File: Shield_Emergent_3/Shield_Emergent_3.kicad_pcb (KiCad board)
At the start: 2 copper layers, 17 parts, among them J1 USB3_B_Micro, J2 Conn_02x08_Odd_Even, J3 USB3_B_Micro, U3 SP3012-06UTG, U4 SP3012-06UTG, X1 USB_C_24pins

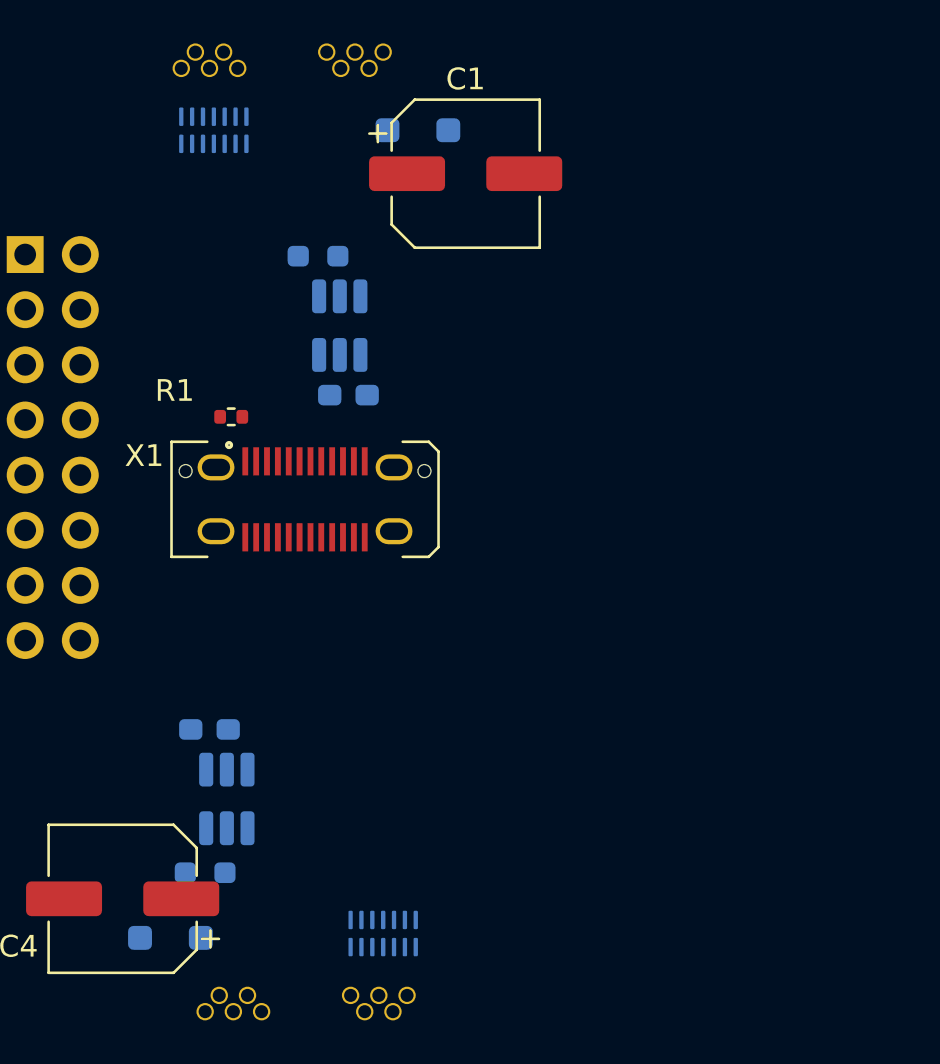
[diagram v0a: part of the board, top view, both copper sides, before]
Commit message: v0.7 nets were modified footprints were corrected Rdy 4 decomposition.
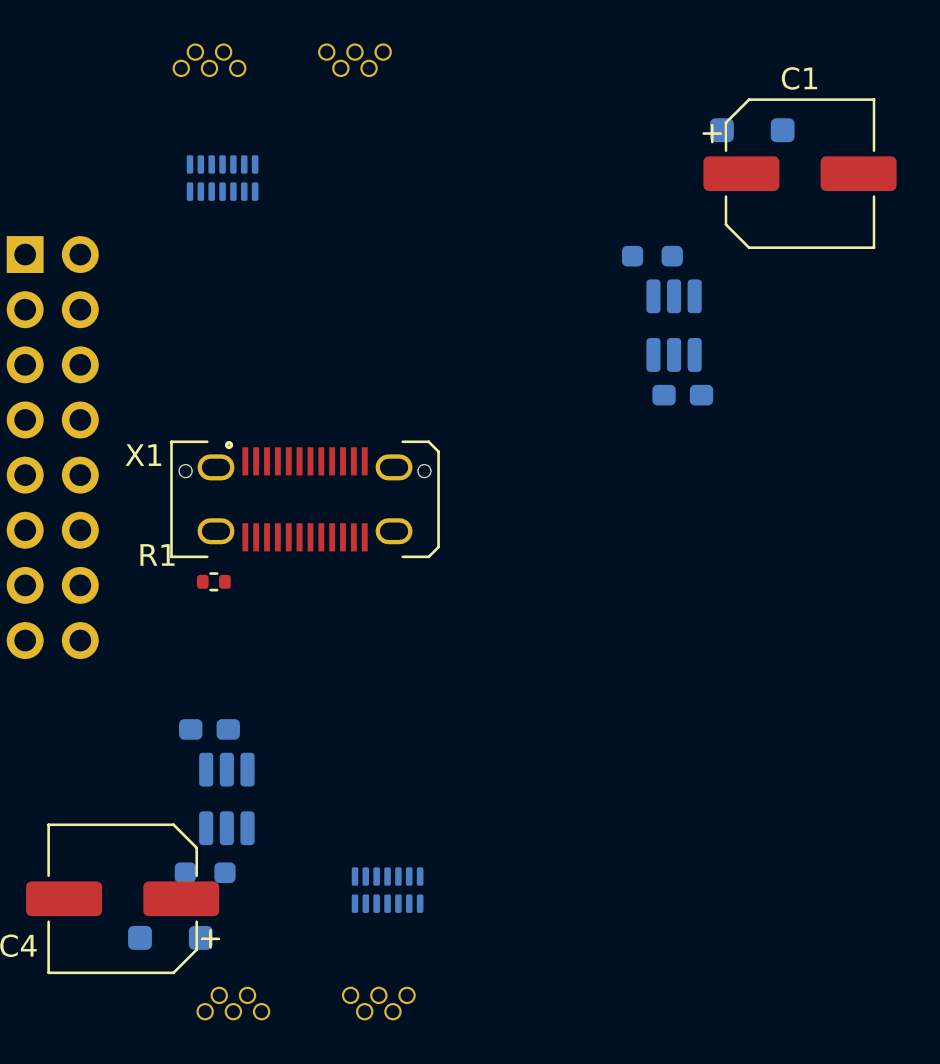
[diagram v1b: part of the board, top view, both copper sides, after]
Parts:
- U3, U4: footprint Package_DFN_QFN:DFN-14_1.35x3.5mm_P0.5mm -> myLib8:DFN-14_1.35x3.5mm_P0.5mm
- moved C1 15.4 mm to (110.4, 25.6)
- moved C2 15.4 mm to (105.0, 35.8)
- moved D1 15.4 mm to (108.2, 23.6)
- moved R4 15.4 mm to (103.6, 29.4)
- moved U1 15.4 mm to (104.6, 32.6)
- moved R1 7.64 mm to (83.4, 44.4)
- moved U3 2.24 mm to (83.8, 25.8)
- moved U4 2.01 mm to (91.4, 58.6)
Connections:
- U3 pad 1: TX1+ -> RX1+
- U3 pad 11: RX1- -> TX1-
- U3 pad 12: RX1+ -> TX1+
- U3 pad 13: TX1- -> RX1-
- U3 pad 14: TX1+ -> RX1+
- U3 pad 2: TX1- -> RX1-
- U3 pad 3: RX1+ -> TX1+
- U3 pad 4: RX1- -> TX1-
- U4 pad 1: TX2+ -> TX2-
- U4 pad 13: TX2- -> TX2+
- U4 pad 14: TX2+ -> TX2-
- U4 pad 2: TX2- -> TX2+

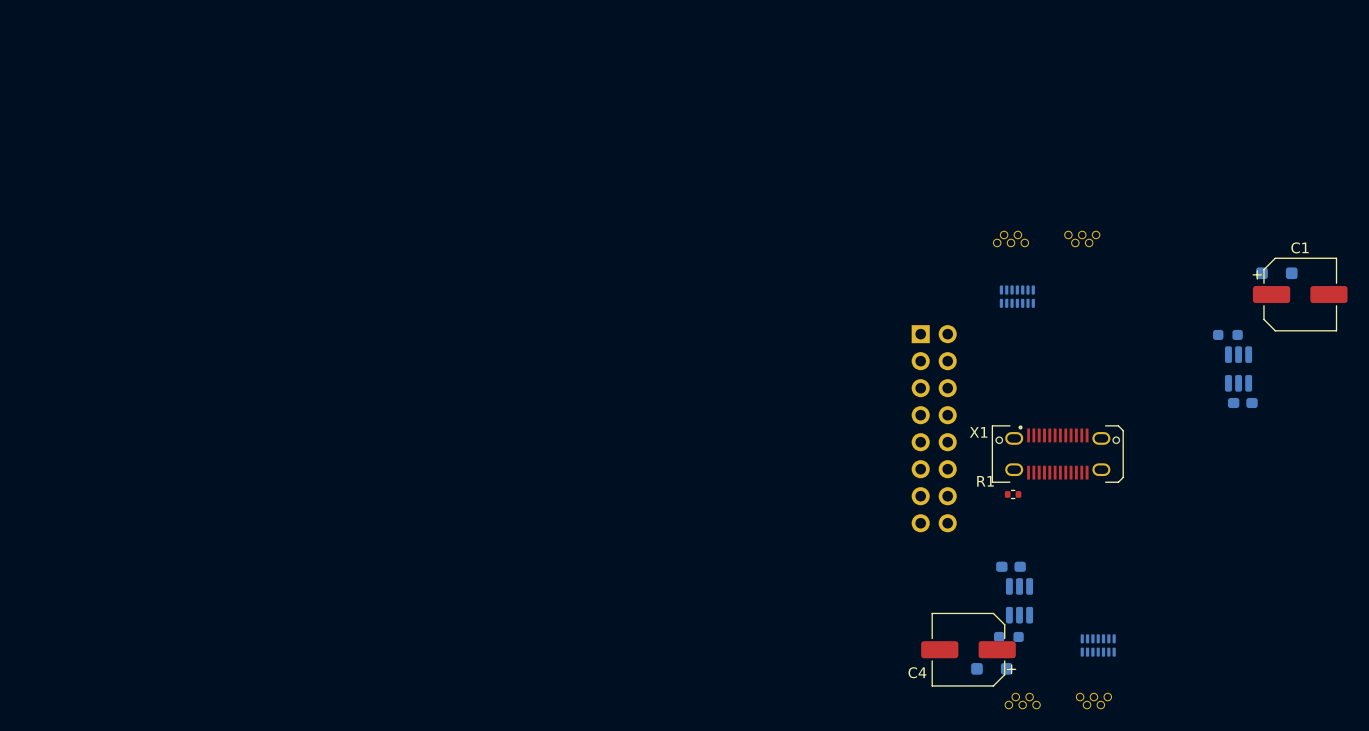
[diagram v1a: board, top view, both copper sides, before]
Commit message: v0.8 Partial decomposition was completed
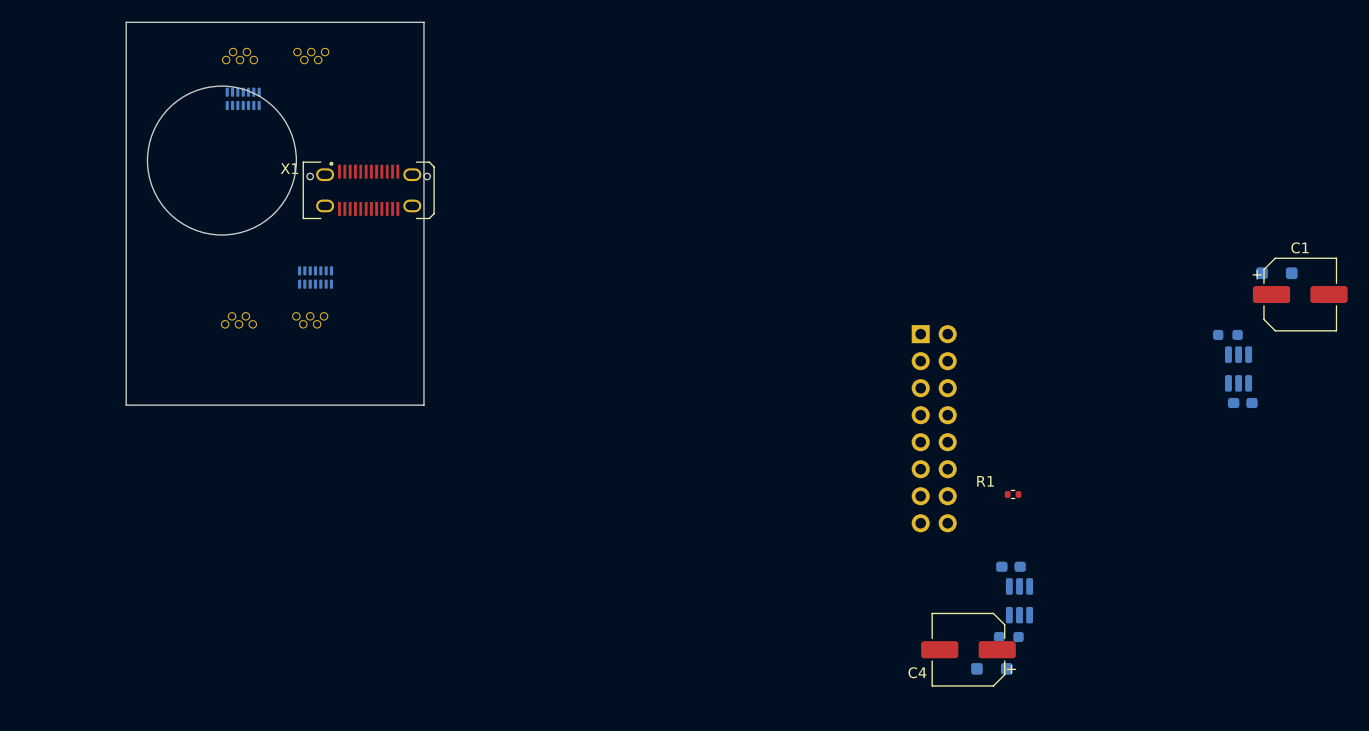
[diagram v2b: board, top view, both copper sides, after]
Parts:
- moved J3 81.9 mm to (9.30, 28.4)
- moved U4 81.3 mm to (17.8, 24.0), turned to 90 degrees
- moved U3 75.1 mm to (11.0, 7.20)
- moved J1 74.5 mm to (18.7, 2.80)
- moved X1 69.4 mm to (22.8, 15.8)
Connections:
- J3 pad 6: TX2- -> TX2+
- J3 pad 7: TX2+ -> TX2-
- U4 pad 1: TX2- -> RX2+
- U4 pad 11: RX2- -> TX2+
- U4 pad 12: RX2+ -> TX2-
- U4 pad 13: TX2+ -> RX2-
- U4 pad 14: TX2- -> RX2+
- U4 pad 2: TX2+ -> RX2-
- U4 pad 3: RX2+ -> TX2-
- U4 pad 4: RX2- -> TX2+
- X1 pad B2: TX2+ -> TX2-
- X1 pad B3: TX2- -> TX2+
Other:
- board outline added: 28 x 36 mm

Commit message: v0.9 Decomposition seems 2B completed
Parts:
- J2: value Conn_02x08_Odd_Even -> Conn_02x04_Odd_Even; footprint Connector_PinSocket_2.54mm:PinSocket_2x08_P2.54mm_Vertical -> Connector_PinHeader_2.54mm:PinHeader_2x04_P2.54mm_Vertical
- moved R4 90.0 mm to (16.2, 7.80), turned to -90 degrees
- moved D1 88.8 mm to (22.0, 2.40), turned to 90 degrees
- moved U1 88.7 mm to (19.4, 7.80), turned to 180 degrees
- moved C1 88.4 mm to (24.4, 5.20), turned to -90 degrees
- moved C2 87.0 mm to (22.6, 7.80), turned to -90 degrees
- moved U2 86.3 mm to (3.00, 24.6)
- moved C3 86.1 mm to (2.40, 21.4)
- moved R8 84.7 mm to (3.80, 27.8), turned to 0 degrees
- moved D2 83.6 mm to (6.00, 24.6), turned to 90 degrees
- moved C4 80.4 mm to (3.80, 31.0), turned to -90 degrees
- moved R1 62.1 mm to (26.6, 19.4), turned to 180 degrees
- moved J2 49.3 mm to (25.9, 22.8)
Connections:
- J2 pad 1: VBUS -> VOUT1
- J2 pad 2: VBUS -> VOUT2
- J2 pad 3: VBUS -> EN1
- J2 pad 4: VBUS -> EN2
- J2 pad 5: GND -> nFLT1
- J2 pad 6: GND -> nFLT2
- J2 pad 7: GND -> BTN1
- J2 pad 8: GND -> BTN2

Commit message: v1.0 Geometry was modified
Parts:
- C2, C3, D1, D2, R4, R8, U1, U2: moved to F.Cu
- moved C1 30.8 mm to (-6.40, 4.40)
- moved J2 16.1 mm to (19.4, 37.5), turned to -90 degrees
- moved C4 15.1 mm to (15.8, 21.8)
- moved C3 10.0 mm to (3.20, 31.4), turned to -90 degrees
- moved R1 8.40 mm to (18.4, 21.2), turned to -90 degrees
- moved U2 7.87 mm to (6.60, 31.6), turned to 0 degrees
- moved R8 7.62 mm to (10.4, 31.6), turned to -90 degrees
- moved C2 6.40 mm to (16.2, 7.80)
- moved R4 6.40 mm to (22.6, 7.80)
- moved J1 4.75 mm to (23.3, 1.60)
- moved U3 4.44 mm to (15.4, 7.80)
- moved D1 2.33 mm to (23.2, 4.40), turned to 0 degrees
- moved X1 2.24 mm to (22.4, 18.0), turned to -90 degrees
- moved D2 1.34 mm to (7.20, 24.0), turned to 180 degrees
- moved U4 0.82 mm to (17.0, 23.8)
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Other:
- board size 28 x 36 mm -> 23.6 x 33.6 mm

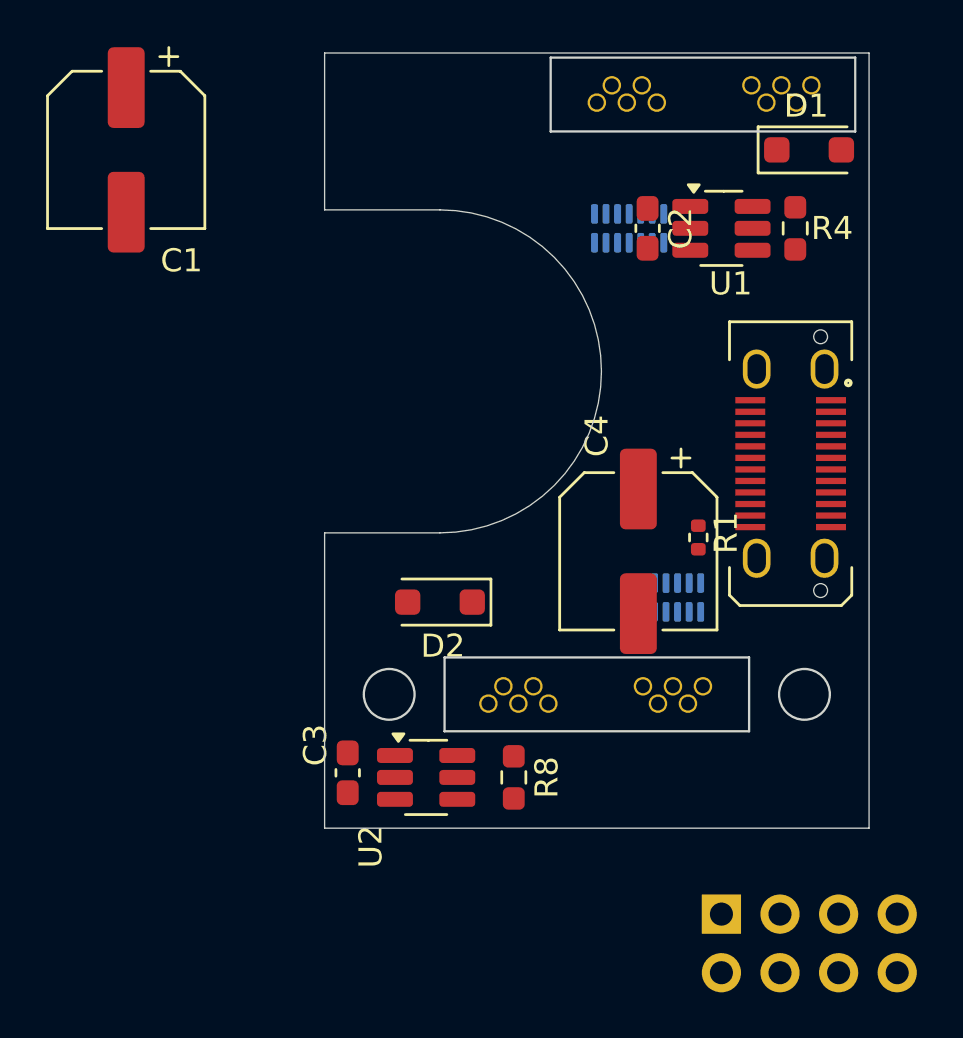
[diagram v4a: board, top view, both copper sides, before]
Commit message: v1.1 Geometry was established, LF routing was completed
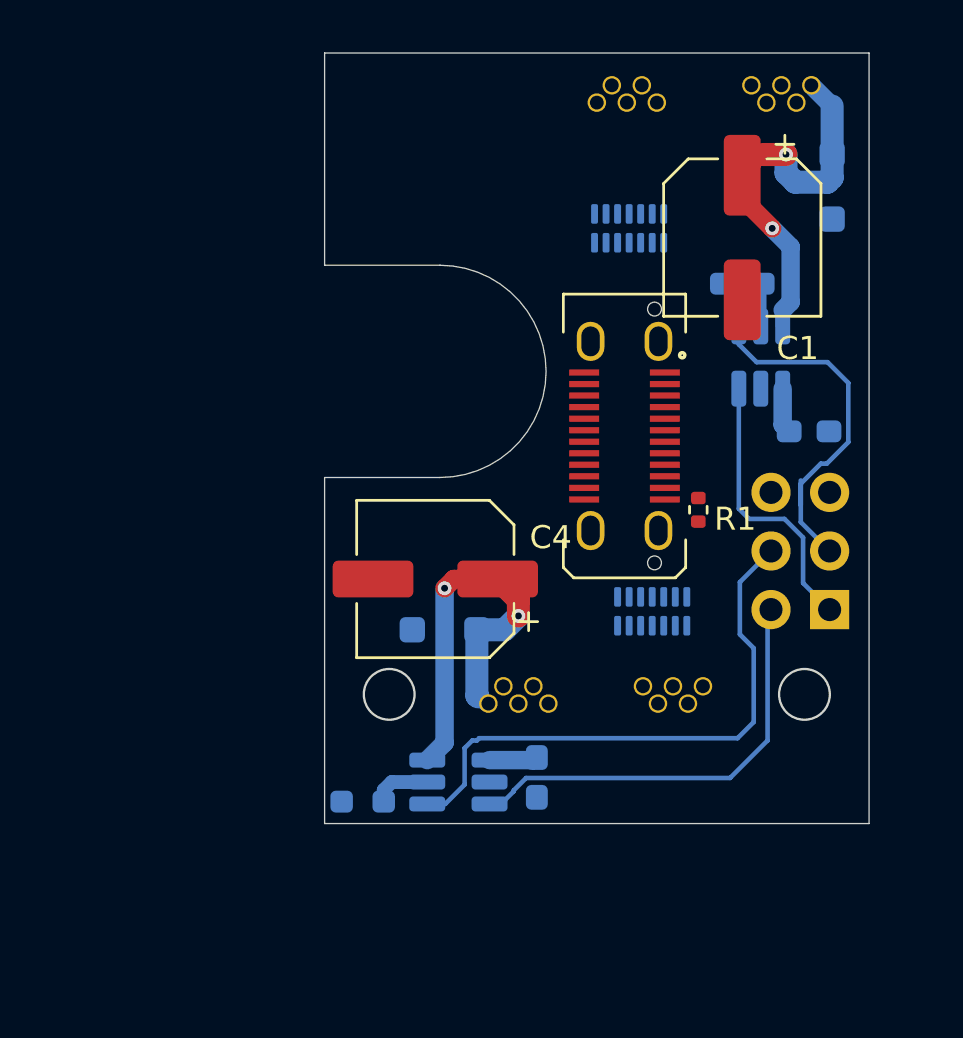
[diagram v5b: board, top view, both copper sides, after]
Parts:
- C2, C3, D1, D2, R4, R8, U1, U2: moved to B.Cu
- J2: value Conn_02x04_Odd_Even -> Conn_02x03_Odd_Even; footprint Connector_PinHeader_2.54mm:PinHeader_2x04_P2.54mm_Vertical -> Connector_PinSocket_2.54mm:PinSocket_2x03_P2.54mm_Vertical
- moved C1 27.0 mm to (20.3, 8.20)
- moved J2 14.0 mm to (24.1, 24.3), turned to 0 degrees
- moved C2 11.2 mm to (23.2, 16.6), turned to 0 degrees
- moved C4 8.88 mm to (7.00, 23.0), turned to 180 degrees
- moved C3 8.20 mm to (11.4, 31.6)
- moved X1 7.30 mm to (15.2, 16.8)
- moved R8 6.63 mm to (3.85, 32.6), turned to 180 degrees
- moved U1 5.85 mm to (21.1, 13.4), turned to 90 degrees
- moved R4 3.32 mm to (20.3, 10.2), turned to 180 degrees
- moved D1 1.89 mm to (24.2, 6.00), turned to -90 degrees
- moved U2 1.41 mm to (8.00, 31.8), turned to 180 degrees
- moved D2 1.22 mm to (7.40, 25.2)
- moved R1 1.20 mm to (18.4, 20.0)
- moved U4 0.85 mm to (16.4, 24.4)
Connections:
- J2 pad 1: VOUT1 -> EN1
- J2 pad 2: VOUT2 -> EN2
- J2 pad 3: EN1 -> nFLT1
- J2 pad 4: EN2 -> nFLT2
- J2 pad 5: nFLT1 -> BTN1
- J2 pad 6: nFLT2 -> BTN2
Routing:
- net nFLT2: track 0.00 -> 24.8 mm
- net EN2: track 0.00 -> 19.0 mm
- net VOUT2: track 0.00 -> 17.8 mm, vias 0 -> 2
- net VOUT1: track 0.00 -> 17.3 mm, vias 0 -> 2
- net nFLT1: track 0.00 -> 16.1 mm
- net EN1: track 0.00 -> 12.1 mm
- net VBUS: track 0.00 -> 4.06 mm
- net Net-(U2-ILIM): track 0.00 -> 2.53 mm
- net Net-(U1-ILIM): track 0.00 -> 1.90 mm
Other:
- board size 23.6 x 33.6 mm -> 23.6 x 33.4 mm
